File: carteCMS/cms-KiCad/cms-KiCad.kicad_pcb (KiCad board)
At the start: 2 copper layers, 100 x 100 mm, 40 parts, among them IC1 CD4093BM, J1 Conn_01x02, J2 Conn_01x16, J3 AVR-ISP-6, J4 HP, SW1 SW_SPDT, SW2 SW-MCIPTG23K-V, SW3 SW-MCIPTG23K-V, SW4 SW-MCIPTG23K-V, U1 LM358, U3 max7426cua+T, U6 ATmega8U2-A, Y2 Crystal

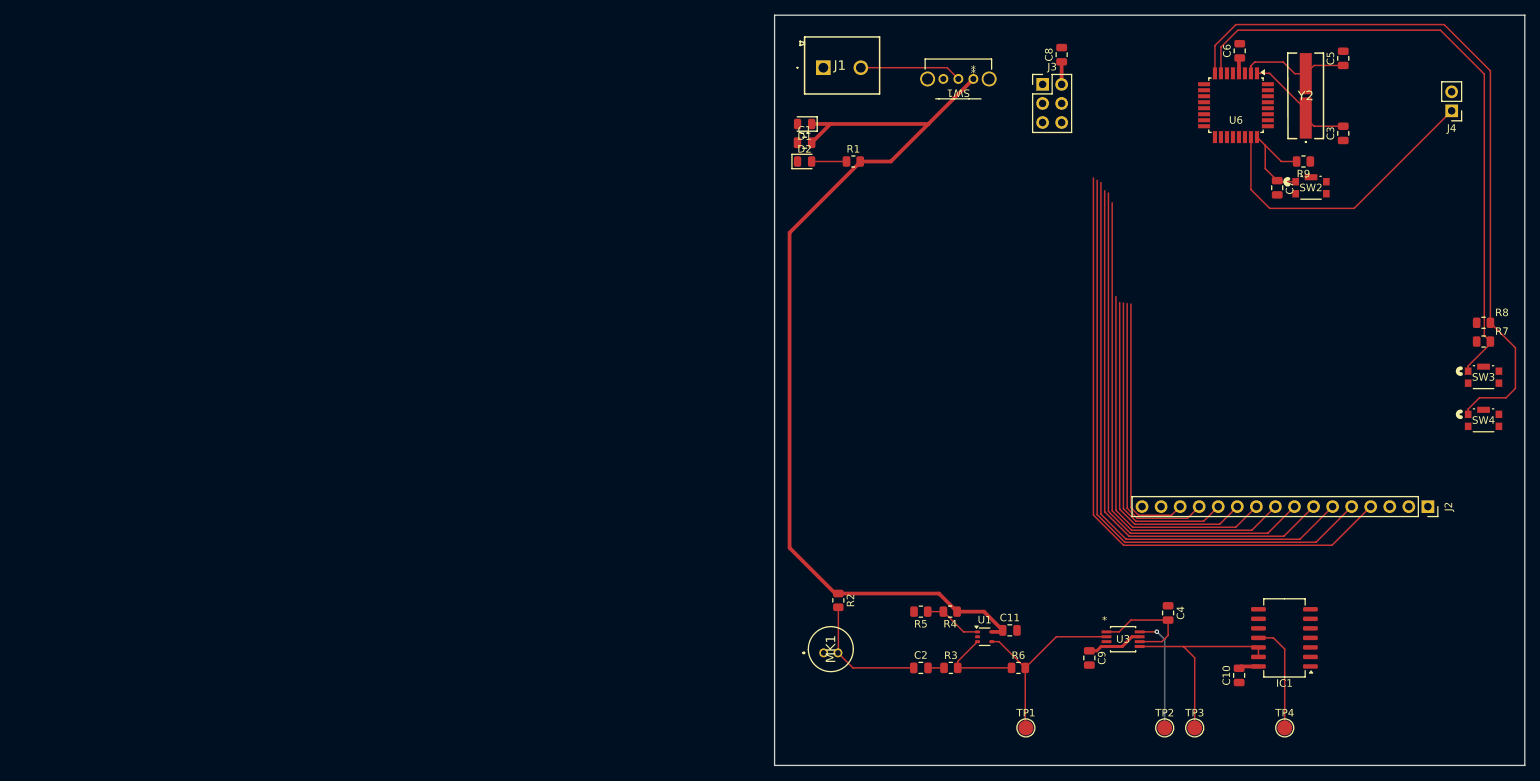
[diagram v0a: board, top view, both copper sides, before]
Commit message: règles à jour - placement sans pistes
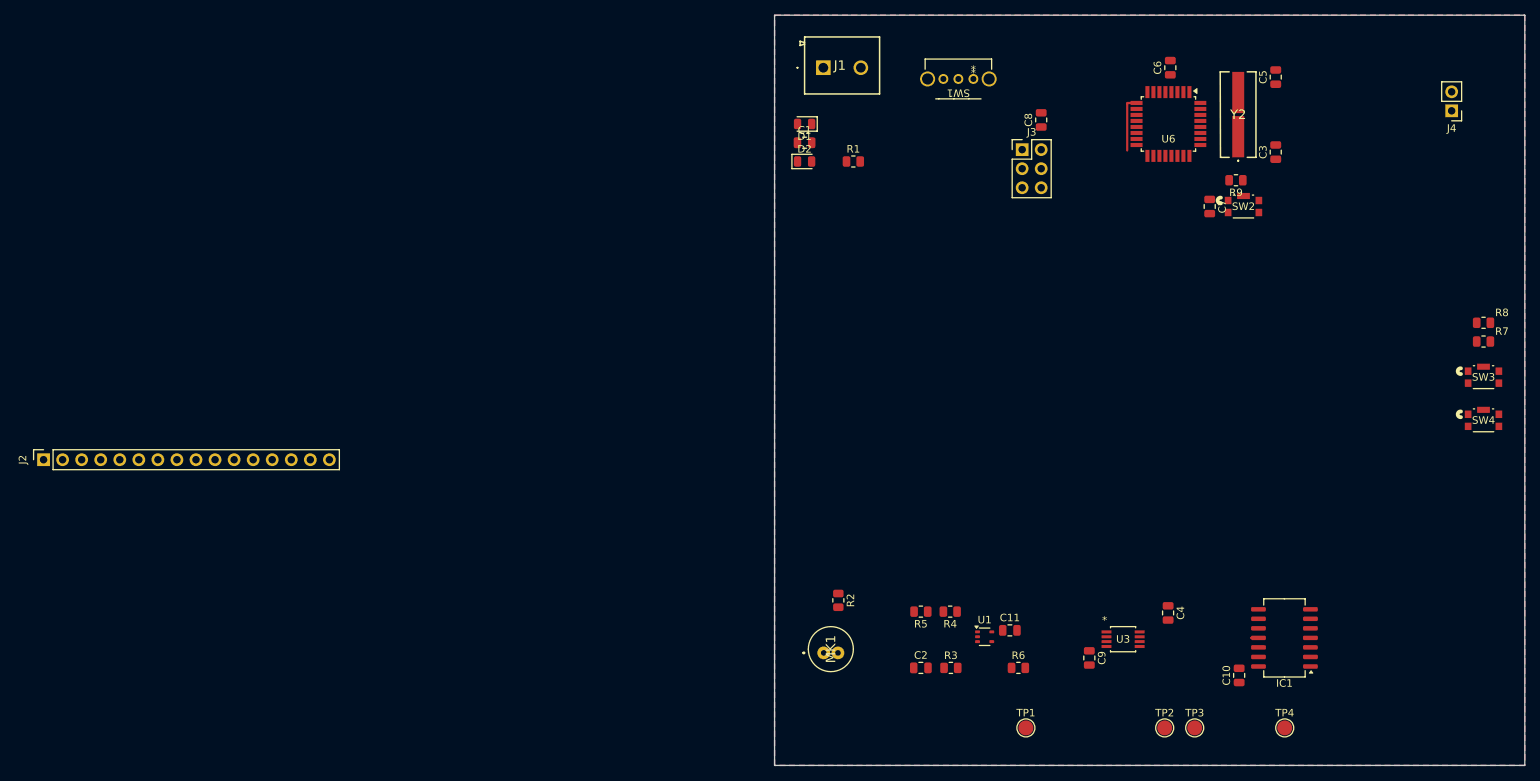
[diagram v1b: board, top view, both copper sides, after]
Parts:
- moved J2 184.6 mm to (27.6, 129.2), turned to 90 degrees
- moved C6 9.52 mm to (177.8, 77.0)
- moved C3 9.34 mm to (191.8, 88.2)
- moved C5 9.34 mm to (191.8, 78.2)
- moved C7 9.34 mm to (183.0, 95.5)
- moved R9 9.34 mm to (186.5, 92.0)
- moved SW2 9.34 mm to (187.5, 95.5)
- moved U6 9.34 mm to (177.5, 84.5)
- moved Y2 9.34 mm to (186.8, 83.2)
- moved J3 9.11 mm to (158.0, 87.9)
- moved C8 9.11 mm to (160.5, 84.0)
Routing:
- net +5V: track 144.3 -> 0.00 mm
- net INT2/PD2: track 96.0 -> 0.00 mm
- net RS: track 85.7 -> 0.00 mm
- net INT1/PD1: track 83.2 -> 0.00 mm
- net R/W: track 82.0 -> 0.00 mm
- net E: track 78.3 -> 0.00 mm
- net Net-(J2-Pin_7): track 73.6 -> 0.00 mm
- net Net-(J2-Pin_8): track 69.9 -> 0.00 mm
- net Net-(J2-Pin_9): track 65.2 -> 0.00 mm
- net Net-(J2-Pin_10): track 49.3 -> 0.00 mm
- net Net-(J2-Pin_11): track 45.0 -> 0.00 mm
- net Net-(J2-Pin_12): track 41.5 -> 0.00 mm
- net Net-(J4-Pin_1): track 40.2 -> 0.00 mm
- net Net-(J2-Pin_13): track 38.1 -> 0.00 mm
- net Net-(J2-Pin_14): track 34.6 -> 0.00 mm
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- added copper zone on B.Cu, net GND
- added copper zone on F.Cu, net GND
